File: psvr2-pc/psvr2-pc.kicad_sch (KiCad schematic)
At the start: 8 parts, among them J1 47272-0001, J2 USB3_B_Micro, J3 Jack-DC, P1 USB_C_Plug, Q1 IRLML6244, U1 RP2040, U2 M95256-WMN6P, Y1 Crystal

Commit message: Figure out KiCad a bit more.
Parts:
- removed J3: Jack-DC, Connector_BarrelJack:BarrelJack_SwitchcraftConxall_RAPC10U_Horizontal, symbol Connector:Jack-DC
- added J4: USB_C_Receptacle_USB2.0_14P, symbol Connector:USB_C_Receptacle_USB2.0_14P
- added U3, U4: FUSB302B01MPX, Package_DFN_QFN:WQFN-14-1EP_2.5x2.5mm_P0.5mm_EP1.45x1.45mm, symbol Interface_USB:FUSB302B01MPX
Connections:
- net GND: now reaches P1.A1 (GND), P1.A12 (GND), P1.B1 (GND), P1.B12 (GND)
- net GND: now also P1.S1 (SHIELD), U1.57 (GND)
- new net: J4.A1 (GND), J4.A12 (GND), J4.B1 (GND), J4.B12 (GND)
- new net: J4.A4 (VBUS), J4.A9 (VBUS), J4.B4 (VBUS), J4.B9 (VBUS)
- new net: J4.A5 (CC1), U4.10 (CC1), U4.11 (CC1)
- new net: J4.B5 (CC2), U4.2 (VBUS)
- new net: U3.1 (CC2), U3.14 (CC2)
- new net: U3.10 (CC1), U3.11 (CC1)
- new net: U3.15 (GND), U3.8 (GND), U3.9 (GND)
- new net: U3.3 (VDD), U3.4 (VDD)
- new net: U4.1 (CC2), U4.14 (CC2)
- new net: U4.15 (GND), U4.8 (GND), U4.9 (GND)
- new net: U4.3 (VDD), U4.4 (VDD)
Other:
- company: (none) -> Swyter
- title: (none) -> PSVR2 to PC adapter
- moved on the sheet: J1, J2, P1, U1, U2, Y1

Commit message: Start connecting wires. I'll probably start using buses and making things tidier.
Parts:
- removed J1: 47272-0001, 47272-0001:MOLEX_47272-0001, symbol 47272-0001:47272-0001
- added J3: DP_47272, LibraryLoader:472720024, symbol DPSwitch-rescue:DP_47272-visclib
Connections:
- net GND: now also J3.11 (GND), J3.16 (GND), J3.2 (GND), J3.5 (GND), J3.8 (GND), J3.MH1, J3.MH2, J3.MH3, J3.MH4
- net at J4.A4 (VBUS), J4.A9 (VBUS), J4.B4 (VBUS)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: now also J4.A5 (CC1), U4.10 (CC1), U4.11 (CC1), U4.2 (VBUS)
- net at J4.A6 (D+): now also J4.B6 (D+)
- net at J4.A7 (D-): now also J4.B7 (D-)
- net at J4.B5 (CC2): now also U4.1 (CC2), U4.14 (CC2); no longer U4.2 (VBUS)
- net at U3.1 (CC2), U3.14 (CC2): now also P1.B5 (VCONN)
- net at U3.10 (CC1), U3.11 (CC1): now also P1.A5 (CC)
- net at U3.2 (VBUS): now also P1.A4 (VBUS), P1.A9 (VBUS), P1.B4 (VBUS), P1.B9 (VBUS)
- net at P1.A10 (RX2-): now also J2.1 (VBUS), J2.10 (SSRX+), J2.2 (D-), J2.3 (D+), J2.4 (ID), J2.6 (SSTX-), J2.7 (SSTX+), J2.9 (SSRX-), P1.A11 (RX2+), P1.B2 (TX2+), P1.B3 (TX2-), U1.44 (VREG_IN), U1.46 (USB_DM), U1.47 (USB_DP)
- net at P1.A2 (TX1+): now also J3.4 (D1_P)
- net at P1.A3 (TX1-): now also J3.6 (D1_N)
- net at P1.B10 (RX1-): now also J3.3 (D0_N)
- net at P1.B11 (RX1+): now also J3.1 (D0_P)
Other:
- moved on the sheet: Q1, U4

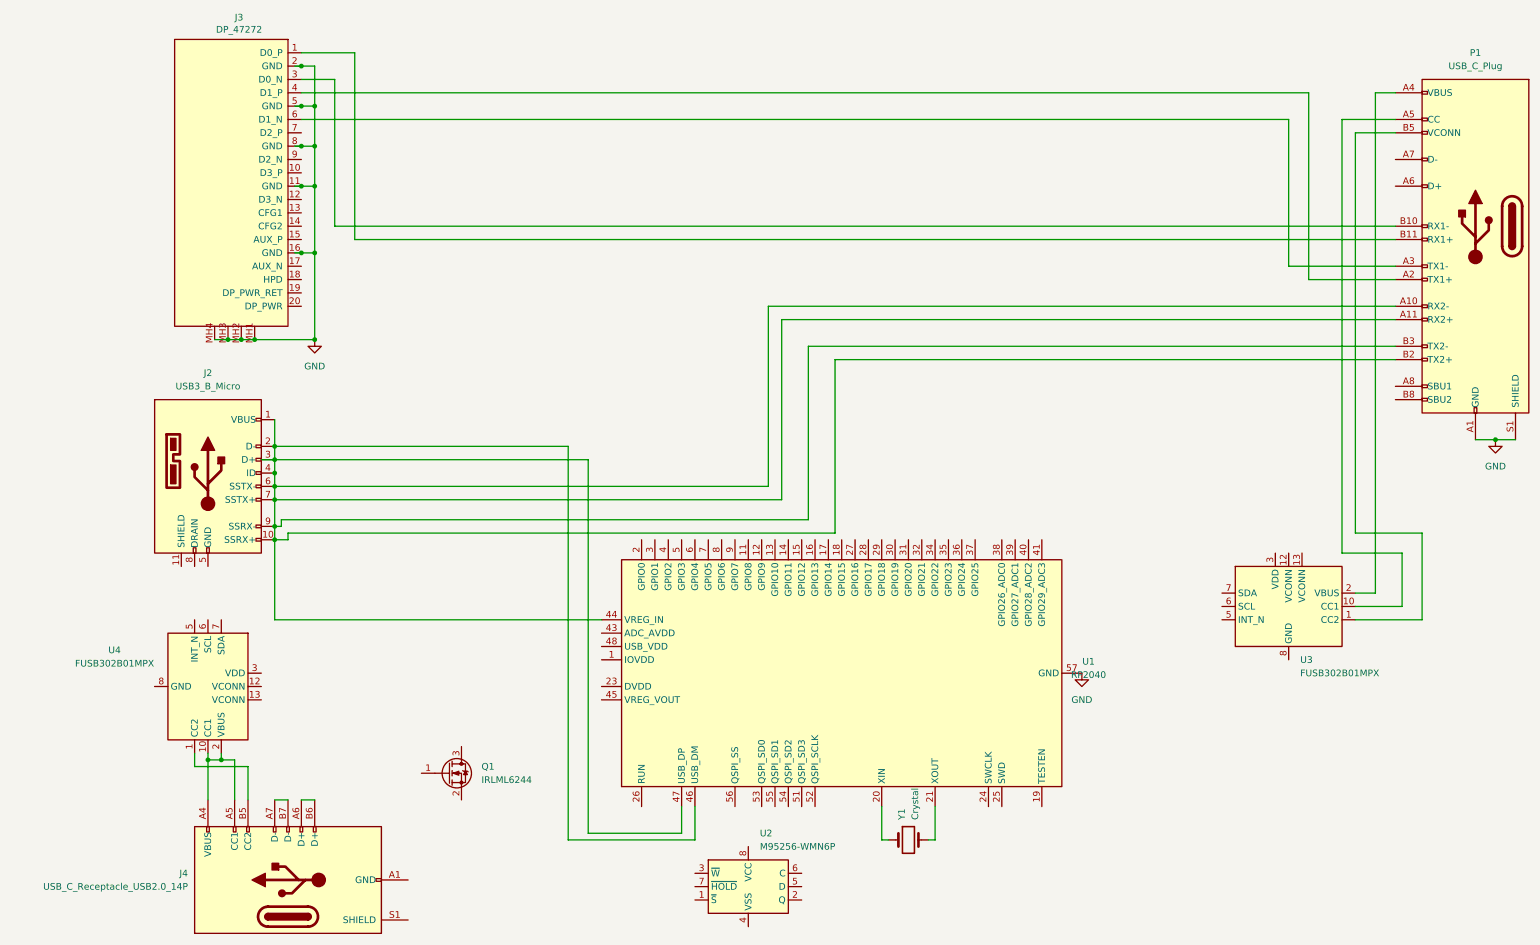
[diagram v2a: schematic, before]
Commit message: Start messing around with buses.
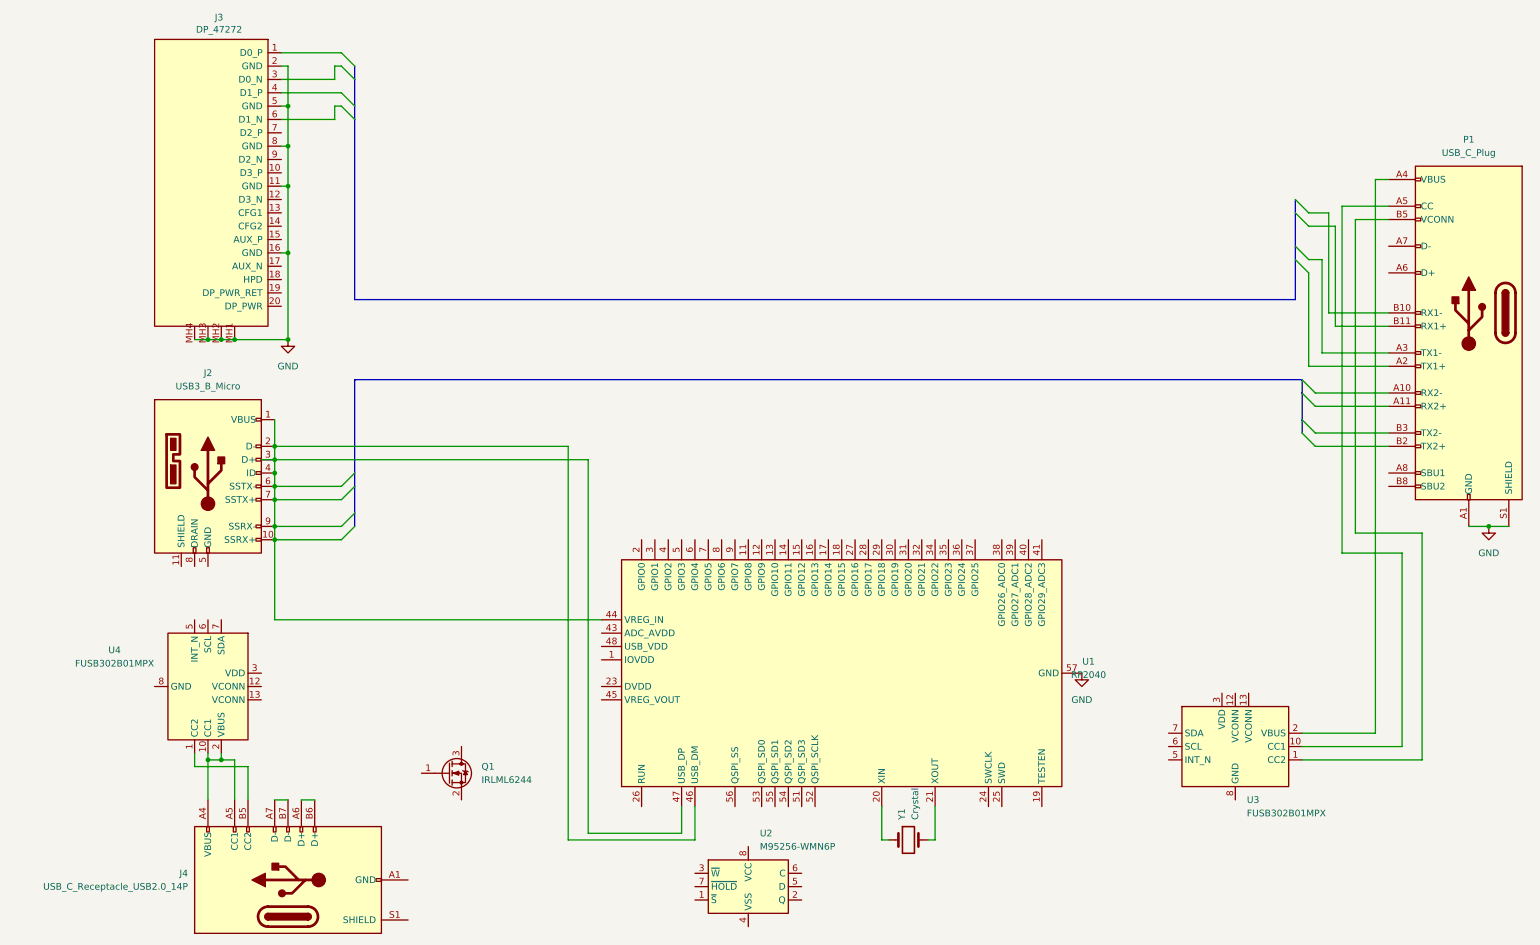
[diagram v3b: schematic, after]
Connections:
- net at J2.1 (VBUS), J2.10 (SSRX+), J2.2 (D-)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: no longer P1.A10 (RX2-), P1.A11 (RX2+), P1.B2 (TX2+), P1.B3 (TX2-)
- net at P1.A2 (TX1+): no longer J3.4 (D1_P)
- net at P1.A3 (TX1-): no longer J3.6 (D1_N)
- net at P1.B10 (RX1-): no longer J3.3 (D0_N)
- net at P1.B11 (RX1+): no longer J3.1 (D0_P)
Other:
- moved on the sheet: J3, P1, U3

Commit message: Start labeling the buses and actually wiring the nets somewhat.
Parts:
- added D1, D2: BAT54GWJ, Diodes_SMD:D_SOD-123, symbol DPSwitch-rescue:BAT54GWJ-visclib
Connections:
- net at J4.A4 (VBUS), J4.A9 (VBUS), J4.B4 (VBUS)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: now also D2.2 (A); no longer J4.A5 (CC1), U4.10 (CC1), U4.11 (CC1), U4.2 (VBUS)
- net PWR_USB2.0_P: now reaches J4.A6 (D+), J4.B6 (D+)
- net PWR_USB2.0_N: now reaches J4.A7 (D-), J4.B7 (D-)
- net SSRX_N: now reaches P1.A10 (RX2-)
- net SSRX_N: now also J2.9 (SSRX-)
- net SSRX_P: now reaches P1.A11 (RX2+)
- net SSRX_P: now also J2.10 (SSRX+)
- net ML1_P: now reaches P1.A2 (TX1+)
- net ML1_P: now also J3.4 (D1_P)
- net ML1_N: now reaches P1.A3 (TX1-)
- net ML1_N: now also J3.6 (D1_N)
- net ML0_N: now reaches P1.B10 (RX1-)
- net ML0_N: now also J3.3 (D0_N)
- net ML0_P: now reaches P1.B11 (RX1+)
- net ML0_P: now also J3.1 (D0_P)
- net SSTX_P: now reaches P1.B2 (TX2+)
- net SSTX_P: now also J2.7 (SSTX+)
- net SSTX_N: now reaches P1.B3 (TX2-)
- net SSTX_N: now also J2.6 (SSTX-)
- new net: J4.A5 (CC1), U4.10 (CC1), U4.11 (CC1)
- new net: D2.1 (K), U4.2 (VBUS)
- new net: D1.2 (A), J2.1 (VBUS)
- new net USB2.0_N: J2.2 (D-)
- now unconnected: J2.3 (D+), J2.4 (ID), U1.44 (VREG_IN), U1.46 (USB_DM), U1.47 (USB_DP)
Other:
- moved on the sheet: U3

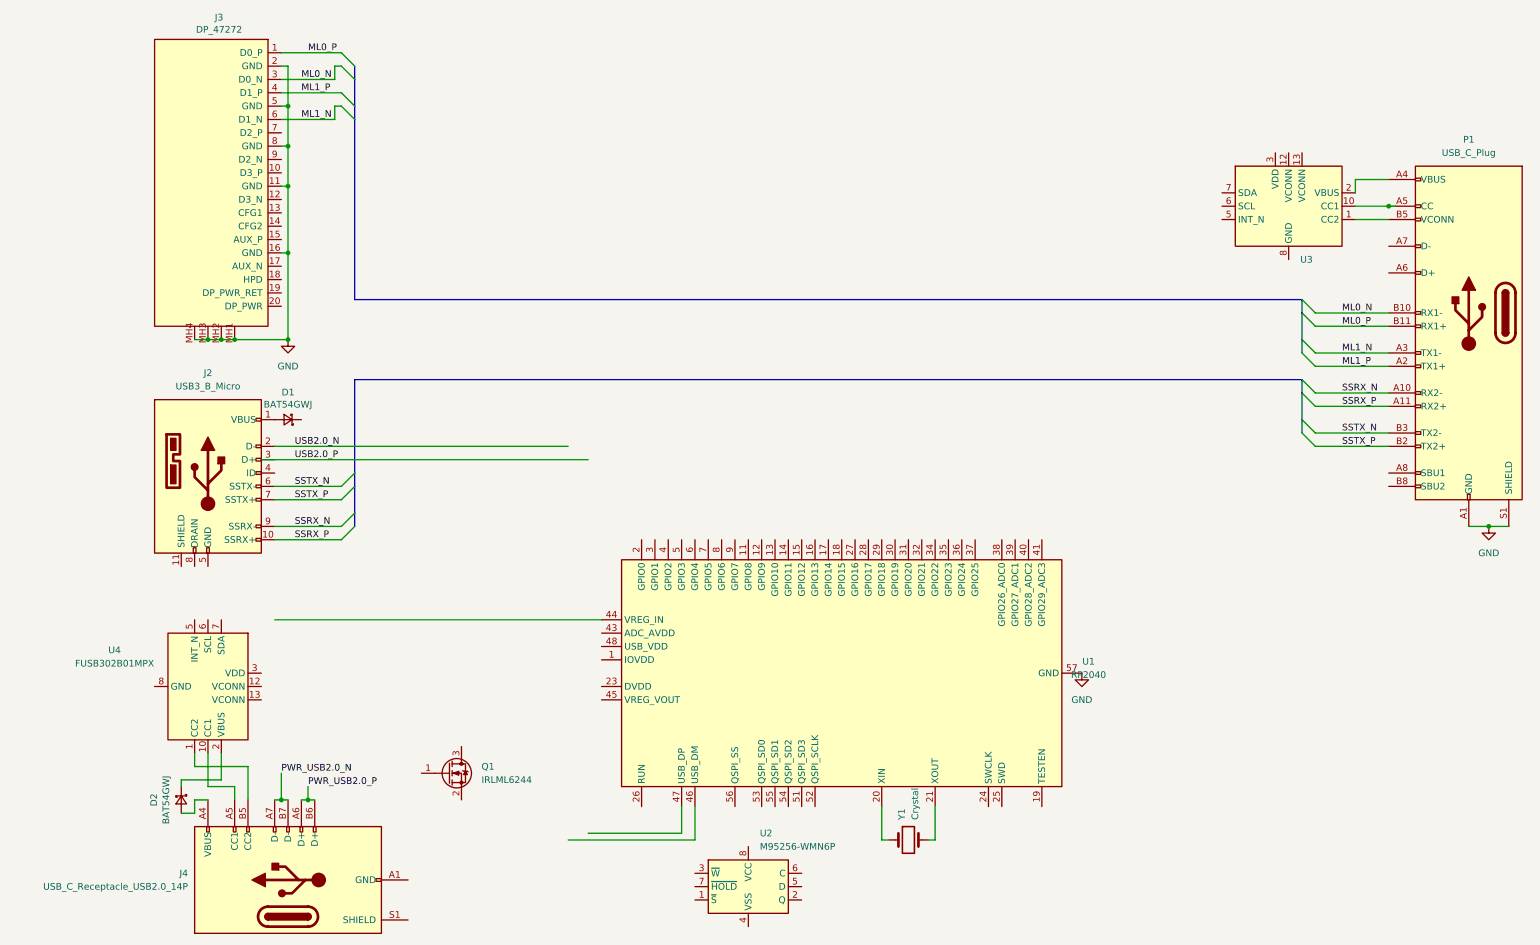
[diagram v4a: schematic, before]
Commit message: Start annotating the DP-alt mode pinouts: https://www.st.com/resource/en/technical_article/ta0356-usb-typec-and-power-delivery-displayport-alternate-mode-stmicroelectronics.pdf
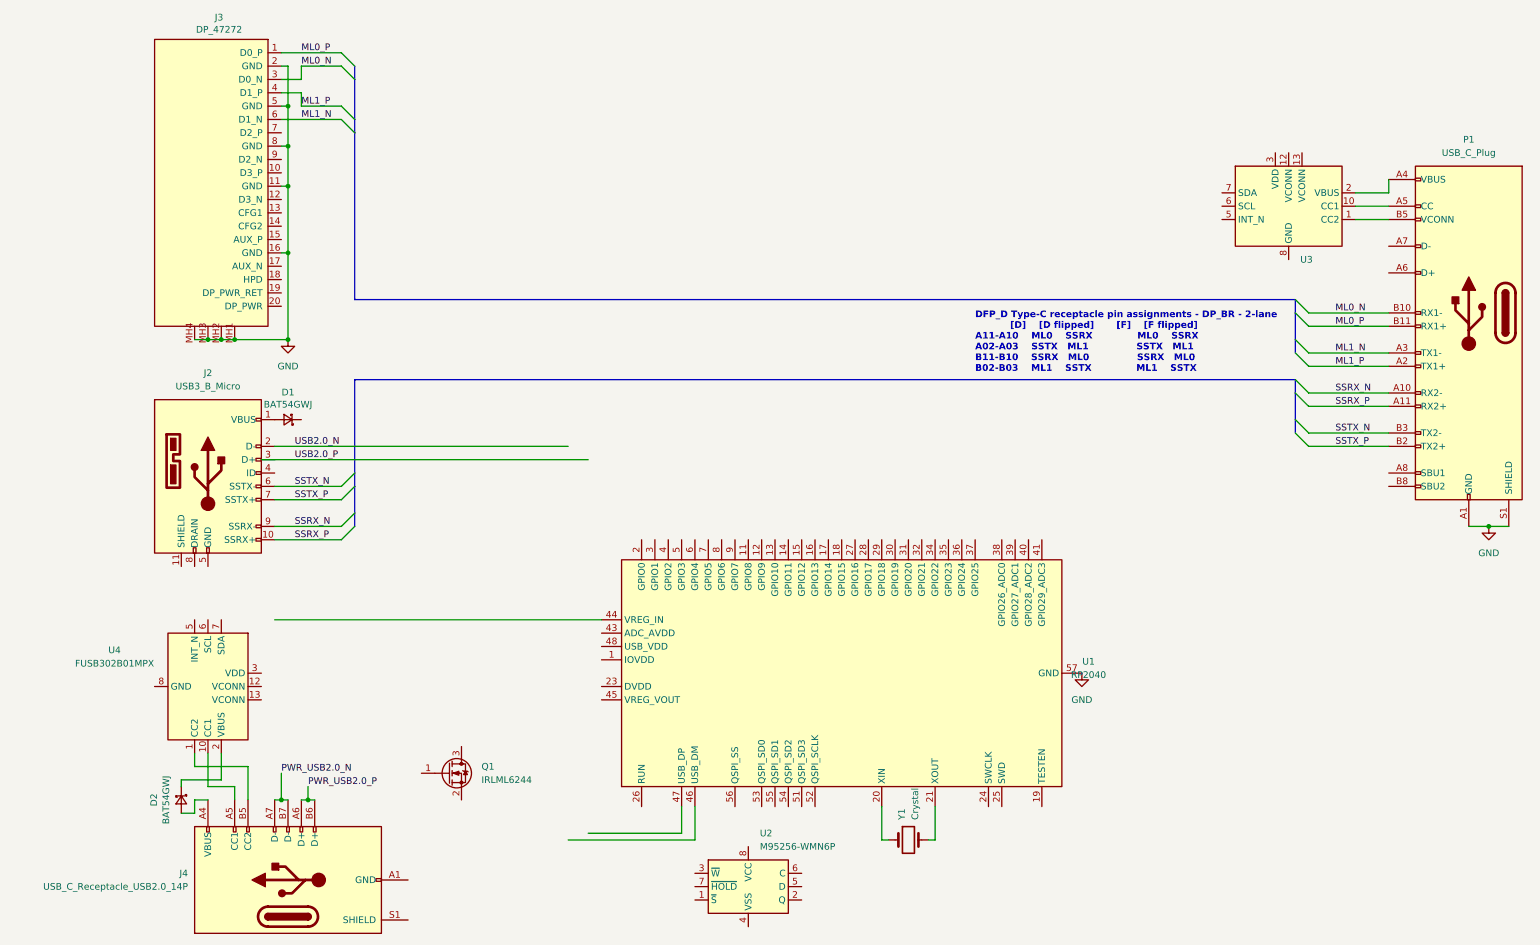
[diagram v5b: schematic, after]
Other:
- note added: "DFP_D Type-C receptacle pin assignments - DP_BR - 2-lane [D] [D flipped] [F] [F flipped] A11-A10 ML0 SSRX ML0 SSRX A02-A03 SSTX ML1 SSTX ML1 B11-B10 SSRX ML0 SSRX ML0 B02-B03 ML1 SSTX ML1 SSTX"
